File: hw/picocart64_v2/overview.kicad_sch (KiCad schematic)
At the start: 0 parts

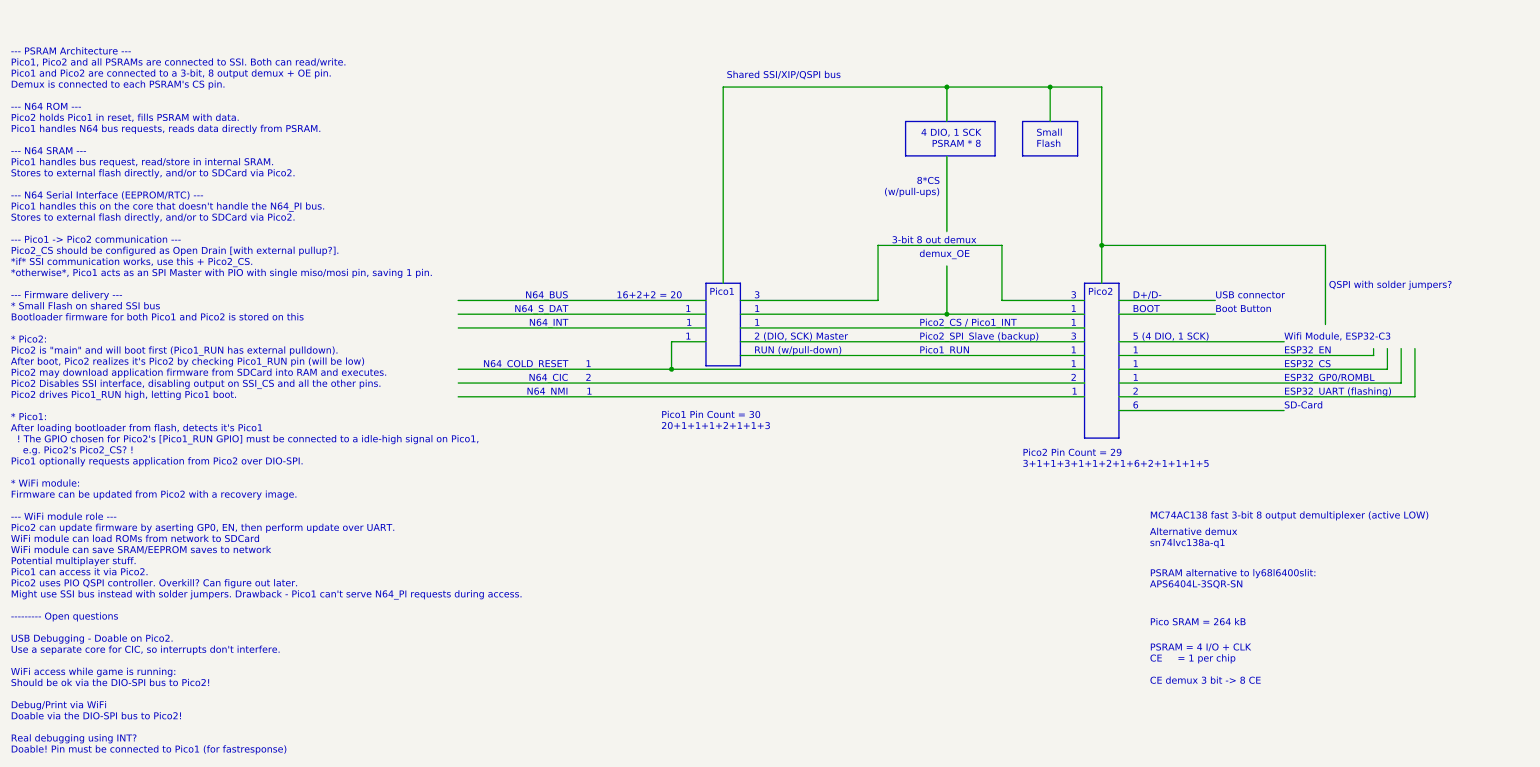
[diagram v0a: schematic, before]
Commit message: Documented and figured out some stuff
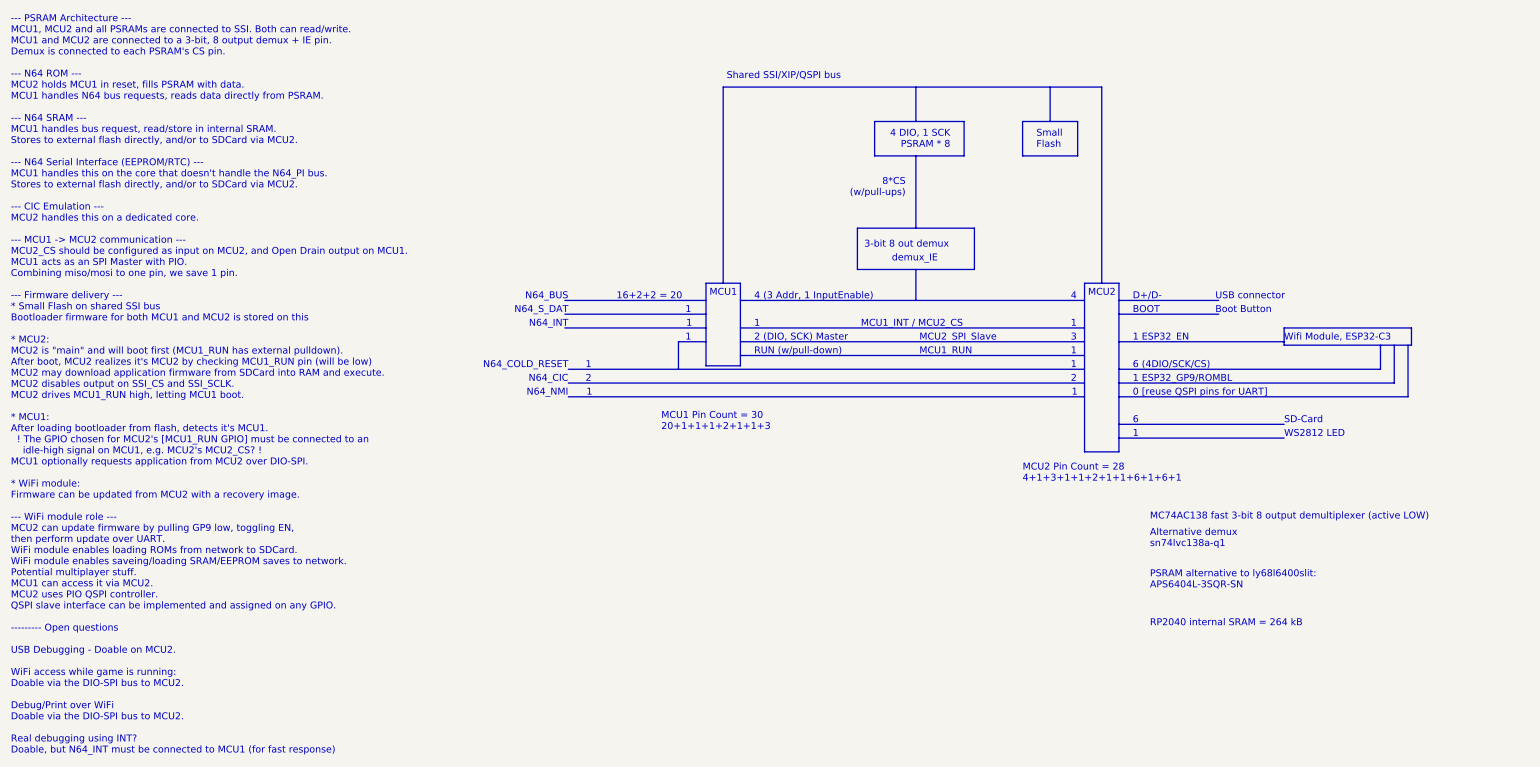
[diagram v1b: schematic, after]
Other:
- note added: "--- PSRAM Architecture --- MCU1, MCU2 and all PSRAMs are connected to SSI. Both can read/write. MCU1 and MCU2 are connected to a 3-bit, 8 output demux + IE pin. Demux is connected to each PSRAM's CS pin. --- N64 ROM --- MCU2 holds MCU1 in reset, fills PSRAM with data. MCU1 handles N64 bus requests, reads data directly from PSRAM. --- N64 SRAM --- MCU1 handles bus request, read/store in internal S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"
- note added: "0 [reuse QSPI pins for UART]"
- note added: "1 ESP32_EN"
- note added: "1 ESP32_GP9/ROMBL"
- note added: "4"
- note added: "4 (3 Addr, 1 InputEnable)"
- note added: "6 (4DIO/SCK/CS)"
- note added: "MCU1"
- note added: "MCU1 Pin Count = 30 20+1+1+1+2+1+1+3"
- note added: "MCU1_INT / MCU2_CS"
- note added: "MCU1_RUN"
- note added: "MCU2"
- note added: "MCU2 Pin Count = 28 4+1+3+1+1+2+1+1+6+1+6+1"
- note added: "MCU2_SPI_Slave"
- note added: "RP2040 internal SRAM = 264 kB"
- note added: "WS2812 LED"
- note added: "demux_IE"
- note removed: "--- PSRAM Architecture --- Pico1, Pico2 and all PSRAMs are connected to SSI. Both can read/write. Pico1 and Pico2 are connected to a 3-bit, 8 output demux + OE pin. Demux is connected to each PSRAM's CS pin. --- N64 ROM --- Pico2 holds Pico1 in reset, fills PSRAM with data. Pico1 handles N64 bus requests, reads data directly from PSRAM. --- N64 SRAM --- Pico1 handles bus request, read/store in in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"
- note removed: "5 (4 DIO, 1 SCK)"
- note removed: "ESP32_CS"
- note removed: "ESP32_EN"
- note removed: "ESP32_GP0/ROMBL"
- note removed: "ESP32_UART (flashing)"
- note removed: "PSRAM = 4 I/O + CLK CE = 1 per chip CE demux 3 bit -> 8 CE"
- note removed: "Pico SRAM = 264 kB"
- note removed: "Pico1"
- note removed: "Pico1 Pin Count = 30 20+1+1+1+2+1+1+3"
- note removed: "Pico1_RUN"
- note removed: "Pico2"
- note removed: "Pico2 Pin Count = 29 3+1+1+3+1+1+2+1+6+2+1+1+1+5"
- note removed: "Pico2_CS / Pico1_INT"
- note removed: "Pico2_SPI_Slave (backup)"
- note removed: "QSPI with solder jumpers?"
- note removed: "demux_OE"
